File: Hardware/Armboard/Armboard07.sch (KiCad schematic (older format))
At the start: 0 parts

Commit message: Added serial pins, limit switches, titles, and indicators
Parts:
- added Conn? (x4): Molex_SL_02, symbol MRDT_Connectors:Molex_SL_02
- added D? (x4): LED, symbol Device:LED
- added R? (x4): 330, symbol Device:R
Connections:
- new net: D?.2 (A), R?.2 (x4)
- new net +3V3: Conn?.1, Conn?.1, Conn?.1, Conn?.1
- new net GND: D?.1 (K), D?.1 (K), D?.1 (K), D?.1 (K)
- new net LS_1: Conn?.2, R?.1
- new net LS_2: Conn?.2, R?.1
- new net LS_3: Conn?.2, R?.1
- new net LS_4: Conn?.2, R?.1
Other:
- note added: "Limit Switches"
- note added: "Yellow"

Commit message: Tiva Updates
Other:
- note added: "Limit Switches and Buttons"
- note removed: "Limit Switches"
- moved on the sheet: Conn?, D?, R?

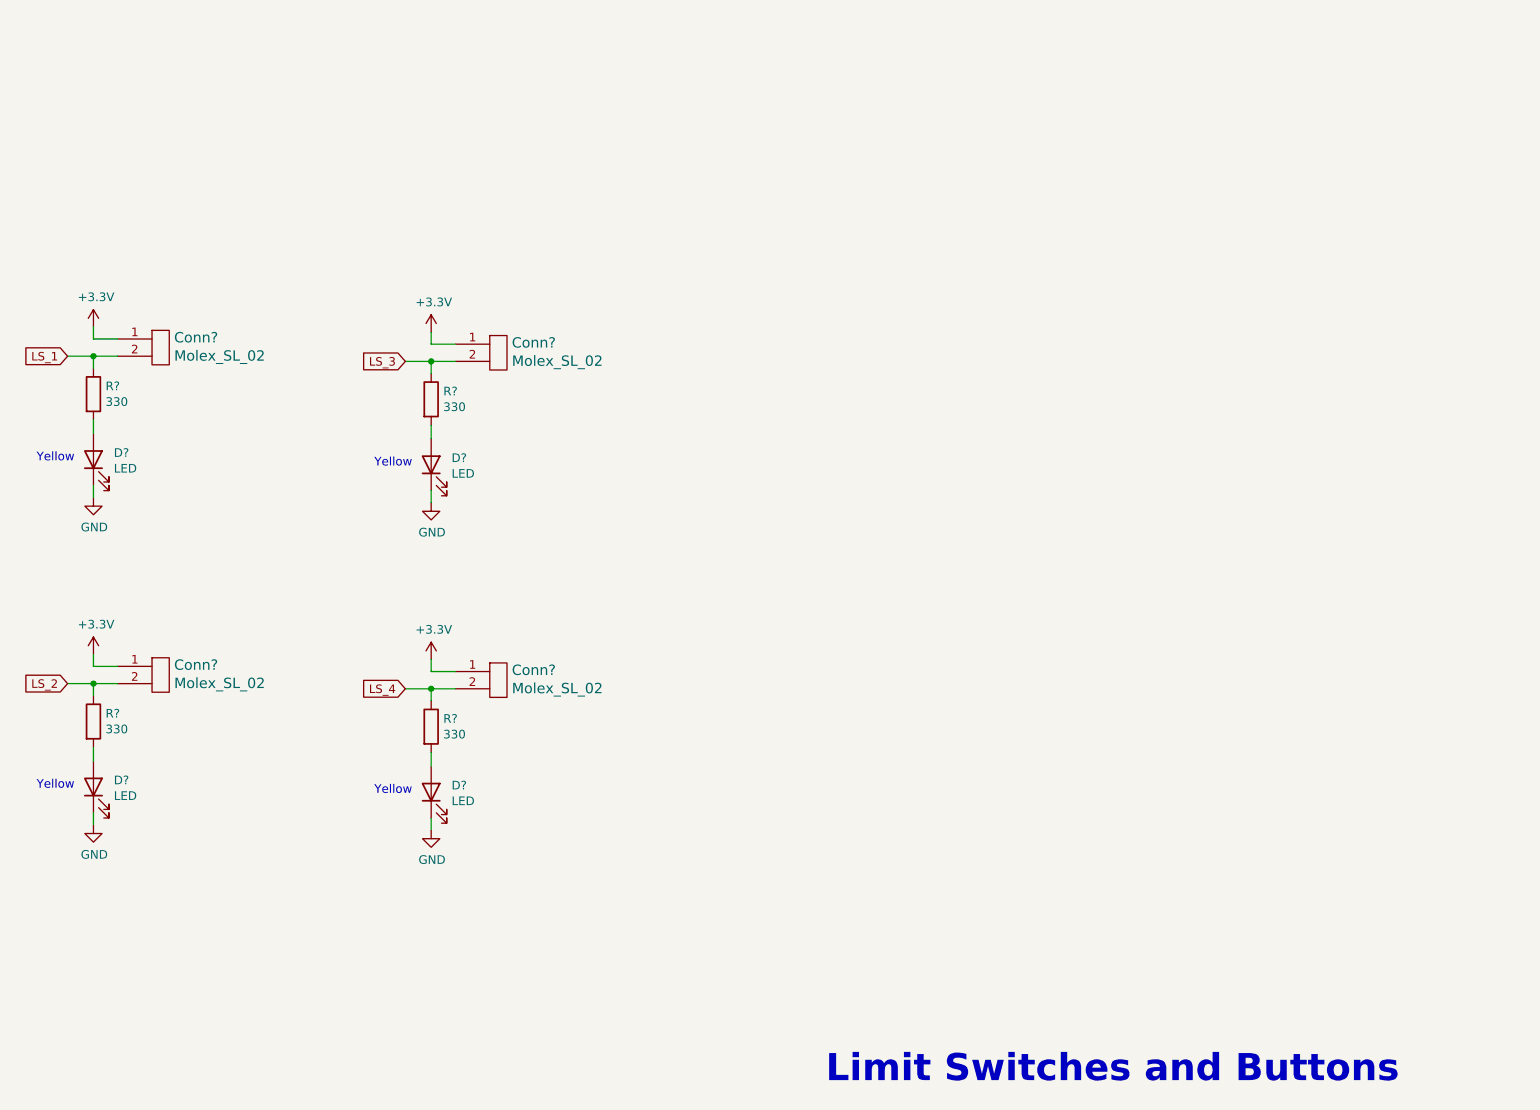
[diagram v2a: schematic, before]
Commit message: Formatted GNDs and added motor toggle buttons
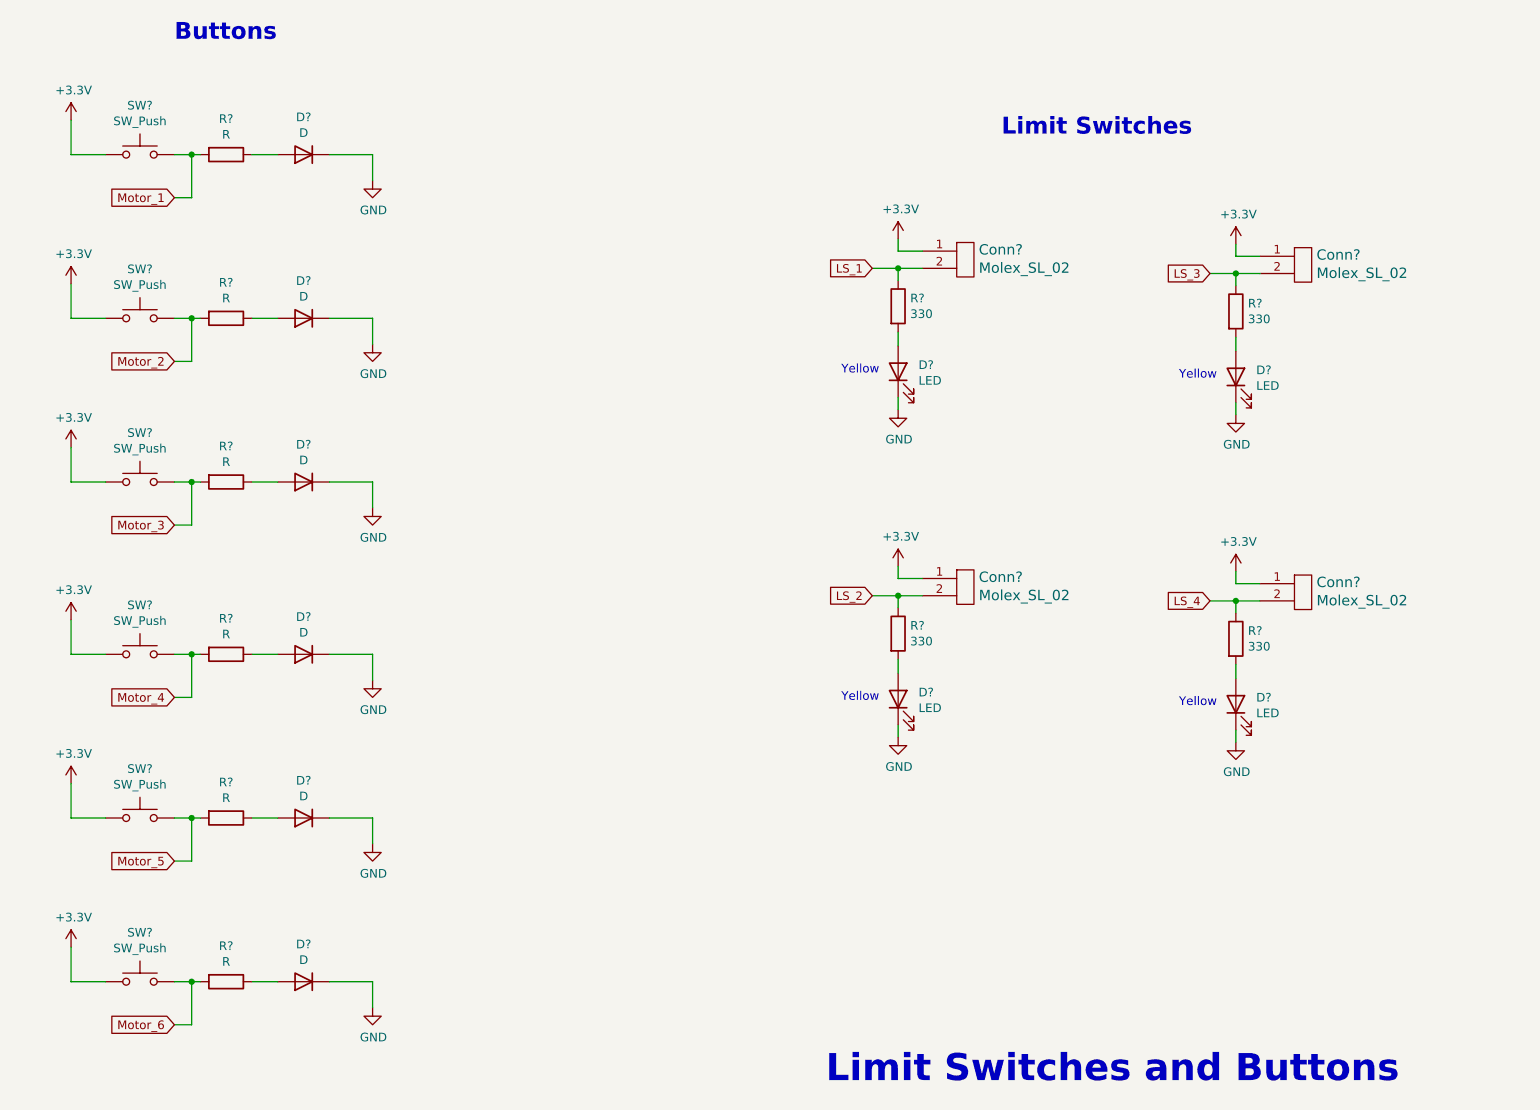
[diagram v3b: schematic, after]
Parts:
- added D? (x6): D, symbol Device:D
- added R? (x6): R, symbol Device:R
- added SW? (x6): SW_Push, symbol Switch:SW_Push
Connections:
- net +3V3: now also SW?.1, SW?.1, SW?.1, SW?.1, SW?.1, SW?.1
- net GND: now also D?.1 (K), D?.1 (K), D?.1 (K), D?.1 (K), D?.1 (K), D?.1 (K)
- new net: D?.2 (A), R?.1 (x6)
- new net Motor_1: R?.2, SW?.2
- new net Motor_2: R?.2, SW?.2
- new net Motor_3: R?.2, SW?.2
- new net Motor_4: R?.2, SW?.2
- new net Motor_5: R?.2, SW?.2
- new net Motor_6: R?.2, SW?.2
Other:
- note added: "Buttons"
- note added: "Limit Switches"
- moved on the sheet: Conn?, D?, R?

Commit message: Moved I/O outside of Power block
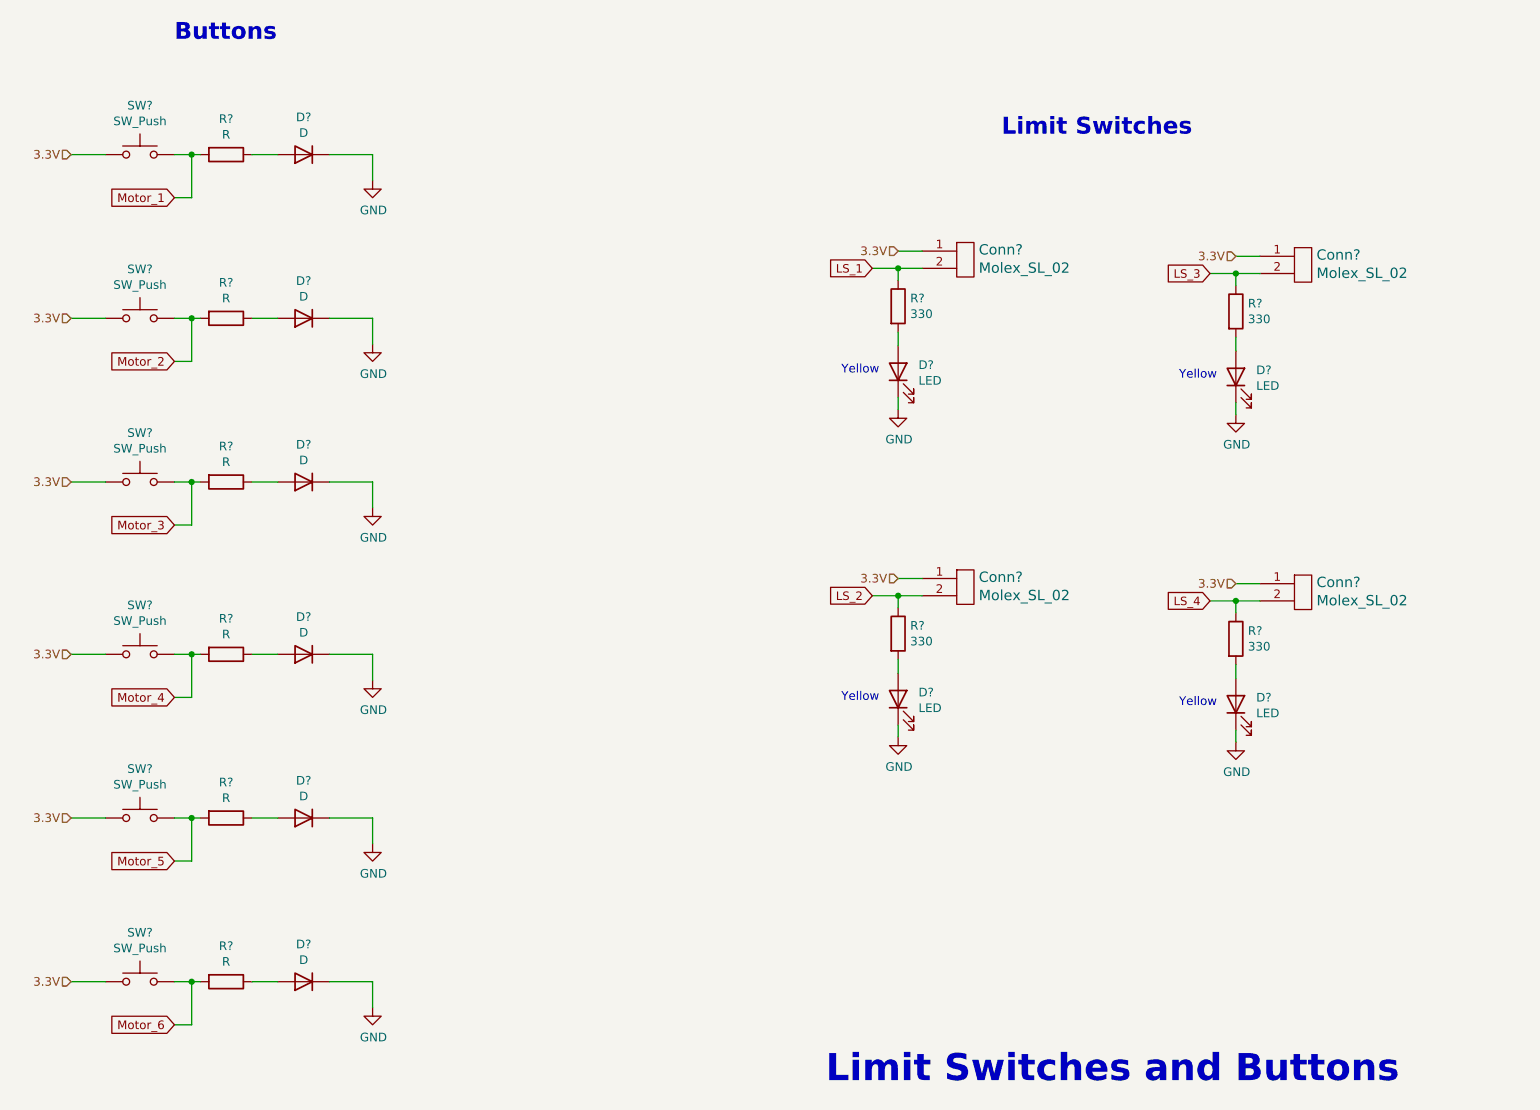
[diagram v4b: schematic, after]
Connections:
- net +3V3 renamed 3.3V
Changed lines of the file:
@@
-	1    0    0    -1
-$EndComp
-$Comp
-L power:+3.3V #PWR?
-U 1 1 5F876076
-P 6950 2240
-F 0 "#PWR?" H 6950 2090 50  0001 C CNN
-F 1 "+3.3V" H 6965 2413 50  0000 C CNN
-F 2 "" H 6950 2240 50  0001 C CNN
-F 3 "" H 6950 2240 50  0001 C CNN
-	1    6950 2240
 	1    0    0    -1
 $EndComp
 Wire Wire Line
 	7090 2310 6950 2310
-Wire Wire Line
-	6950 2310 6950 2240
 Text GLabel 6800 4310 0    49   Input ~ 0
 LS_2
@@
 	1    0    0    -1
 $EndComp
-$Comp
-L power:+3.3V #PWR?
-U 1 1 5F877D1B
-P 6950 4140
-F 0 "#PWR?" H 6950 3990 50  0001 C CNN
-F 1 "+3.3V" H 6965 4313 50  0000 C CNN
-F 2 "" H 6950 4140 50  0001 C CNN
-F 3 "" H 6950 4140 50  0001 C CNN
-	1    6950 4140
-	1    0    0    -1
-$EndComp
 Wire Wire Line
 	7090 4210 6950 4210
-Wire Wire Line
-	6950 4210 6950 4140
 Text GLabel 8760 2440 0    49   Input ~ 0
 LS_3
@@
 	1    0    0    -1
 $EndComp
-$Comp
-L power:+3.3V #PWR?
-U 1 1 5F879724
-P 8910 2270
-F 0 "#PWR?" H 8910 2120 50  0001 C CNN
-F 1 "+3.3V" H 8925 2443 50  0000 C CNN
-F 2 "" H 8910 2270 50  0001 C CNN
-F 3 "" H 8910 2270 50  0001 C CNN
-	1    8910 2270
-	1    0    0    -1
-$EndComp
 Wire Wire Line
 	9050 2340 8910 2340
-Wire Wire Line
-	8910 2340 8910 2270
 Text GLabel 8760 4340 0    49   Input ~ 0
 LS_4
@@
 	1    0    0    -1
 $EndComp
-$Comp
-L power:+3.3V #PWR?
-U 1 1 5F87974C
-P 8910 4170
-F 0 "#PWR?" H 8910 4020 50  0001 C CNN
-F 1 "+3.3V" H 8925 4343 50  0000 C CNN
-F 2 "" H 8910 4170 50  0001 C CNN
-F 3 "" H 8910 4170 50  0001 C CNN
-	1    8910 4170
-	1    0    0    -1
-$EndComp
 Wire Wire Line
 	9050 4240 8910 4240
-Wire Wire Line
-	8910 4240 8910 4170
 Text Notes 6530 7150 0    157  ~ 31
 Limit Switches and Buttons
-$Comp
-L power:+3.3V #PWR?
-U 1 1 5F85F786
-P 2150 1550
-F 0 "#PWR?" H 2150 1400 50  0001 C CNN
-F 1 "+3.3V" H 2165 1723 50  0000 C CNN
-F 2 "" H 2150 1550 50  0001 C CNN
-F 3 "" H 2150 1550 50  0001 C CNN
-	1    2150 1550
-	1    0    0    -1
-$EndComp
 $Comp
 L power:GND #PWR?
@@
 	0    1    1    0
 $EndComp
-Wire Wire Line
-	2150 1550 2150 1750
 Wire Wire Line
 	2150 1750 2350 1750
@@
 $EndComp
 $Comp
-L power:+3.3V #PWR?
-U 1 1 5F86507C
-P 2150 2500
-F 0 "#PWR?" H 2150 2350 50  0001 C CNN
-F 1 "+3.3V" H 2165 2673 50  0000 C CNN
-F 2 "" H 2150 2500 50  0001 C CNN
-F 3 "" H 2150 2500 50  0001 C CNN
-	1    2150 2500
-	1    0    0    -1
-$EndComp
-$Comp
 L power:GND #PWR?
 U 1 1 5F865082
@@
 	0    1    1    0
 $EndComp
-Wire Wire Line
-	2150 2500 2150 2700
 Wire Wire Line
 	2150 2700 2350 2700
@@
 $EndComp
 $Comp
-L power:+3.3V #PWR?
-U 1 1 5F8660F2
-P 2150 3450
-F 0 "#PWR?" H 2150 3300 50  0001 C CNN
-F 1 "+3.3V" H 2165 3623 50  0000 C CNN
-F 2 "" H 2150 3450 50  0001 C CNN
-F 3 "" H 2150 3450 50  0001 C CNN
-	1    2150 3450
-	1    0    0    -1
-$EndComp
-$Comp
 L power:GND #PWR?
 U 1 1 5F8660F8
@@
 	0    1    1    0
 $EndComp
-Wire Wire Line
-	2150 3450 2150 3650
 Wire Wire Line
 	2150 3650 2350 3650
@@
 $EndComp
 $Comp
-L power:+3.3V #PWR?
-U 1 1 5F868CEB
-P 2150 4450
-F 0 "#PWR?" H 2150 4300 50  0001 C CNN
-F 1 "+3.3V" H 2165 4623 50  0000 C CNN
-F 2 "" H 2150 4450 50  0001 C CNN
-F 3 "" H 2150 4450 50  0001 C CNN
-	1    2150 4450
-	1    0    0    -1
-$EndComp
-$Comp
 L power:GND #PWR?
 U 1 1 5F868CF1
@@
 	0    1    1    0
 $EndComp
-Wire Wire Line
-	2150 4450 2150 4650
 Wire Wire Line
 	2150 4650 2350 4650
@@
 $EndComp
 $Comp
-L power:+3.3V #PWR?
-U 1 1 5F868D14
-P 2150 5400
-F 0 "#PWR?" H 2150 5250 50  0001 C CNN
-F 1 "+3.3V" H 2165 5573 50  0000 C CNN
-F 2 "" H 2150 5400 50  0001 C CNN
-F 3 "" H 2150 5400 50  0001 C CNN
-	1    2150 5400
-	1    0    0    -1
-$EndComp
-$Comp
 L power:GND #PWR?
 U 1 1 5F868D1A
@@
 	0    1    1    0
 $EndComp
-Wire Wire Line
-	2150 5400 2150 5600
 Wire Wire Line
 	2150 5600 2350 5600
@@
 $EndComp
 $Comp
-L power:+3.3V #PWR?
-U 1 1 5F868D3D
-P 2150 6350
-F 0 "#PWR?" H 2150 6200 50  0001 C CNN
-F 1 "+3.3V" H 2165 6523 50  0000 C CNN
-F 2 "" H 2150 6350 50  0001 C CNN
-F 3 "" H 2150 6350 50  0001 C CNN
-	1    2150 6350
-	1    0    0    -1
-$EndComp
-$Comp
 L power:GND #PWR?
 U 1 1 5F868D43
@@
 	0    1    1    0
 $EndComp
-Wire Wire Line
-	2150 6350 2150 6550
 Wire Wire Line
 	2150 6550 2350 6550
@@
 Text Notes 2750 1100 0    98   ~ 20
 Buttons
+Text HLabel 2150 1750 0    50   Input ~ 0
+3.3V
+Text HLabel 2150 2700 0    50   Input ~ 0
+3.3V
+Text HLabel 2150 3650 0    50   Input ~ 0
+3.3V
+Text HLabel 2150 4650 0    50   Input ~ 0
+3.3V
+Text HLabel 2150 5600 0    50   Input ~ 0
+3.3V
+Text HLabel 2150 6550 0    50   Input ~ 0
+3.3V
+Text HLabel 6950 4210 0    50   Input ~ 0
+3.3V
+Text HLabel 8910 4240 0    50   Input ~ 0
+3.3V
+Text HLabel 8910 2340 0    50   Input ~ 0
+3.3V
+Text HLabel 6950 2310 0    50   Input ~ 0
+3.3V
 $EndSCHEMATC
